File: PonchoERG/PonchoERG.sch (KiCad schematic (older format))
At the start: 1 part, among them J4 CONN_02X04

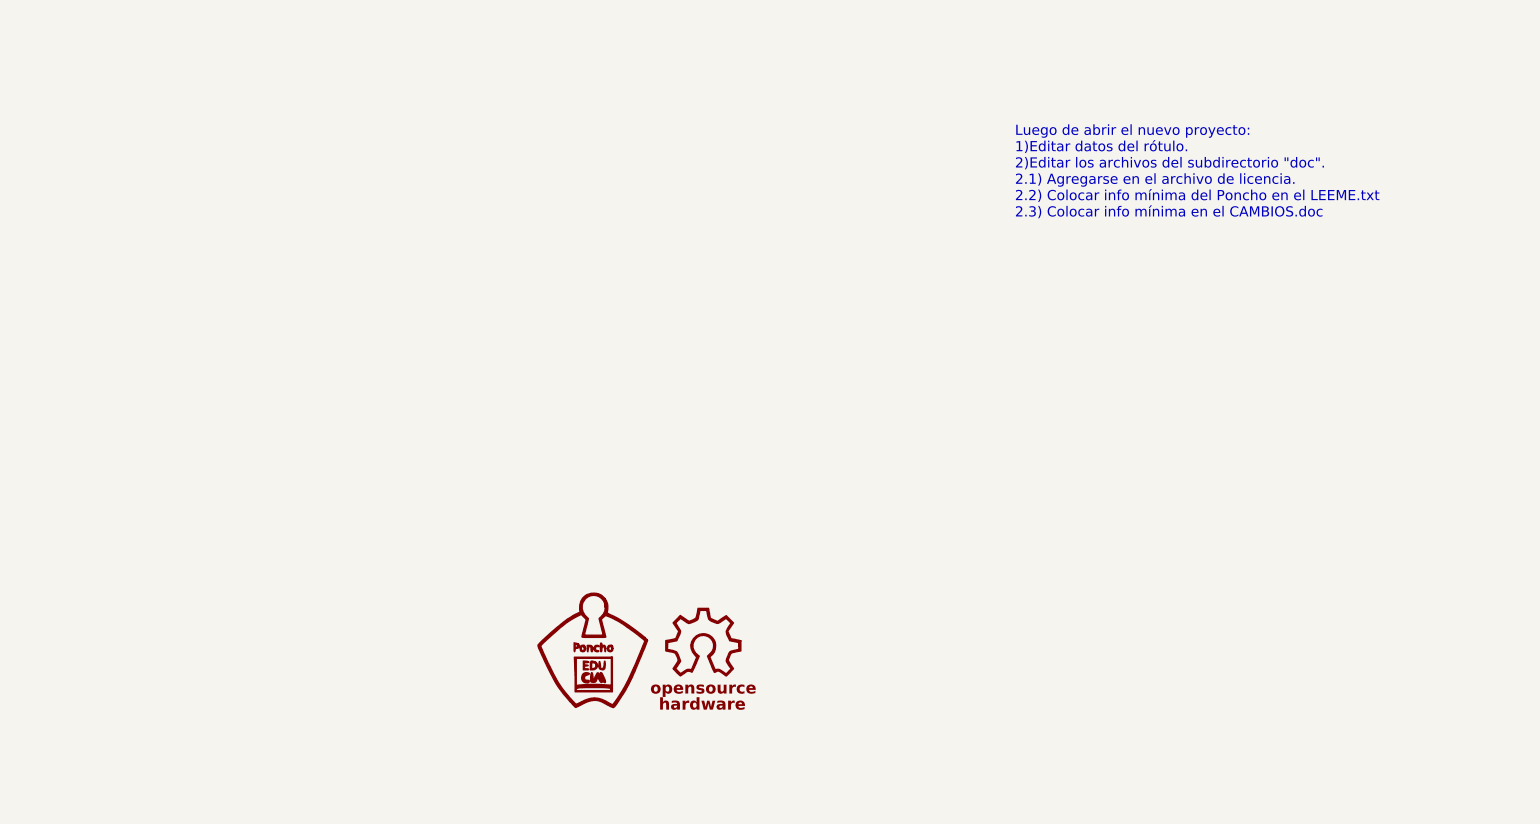
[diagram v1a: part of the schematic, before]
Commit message: Reubicación de ADS y componentes pasivos asociados. Sujeto a revisión.
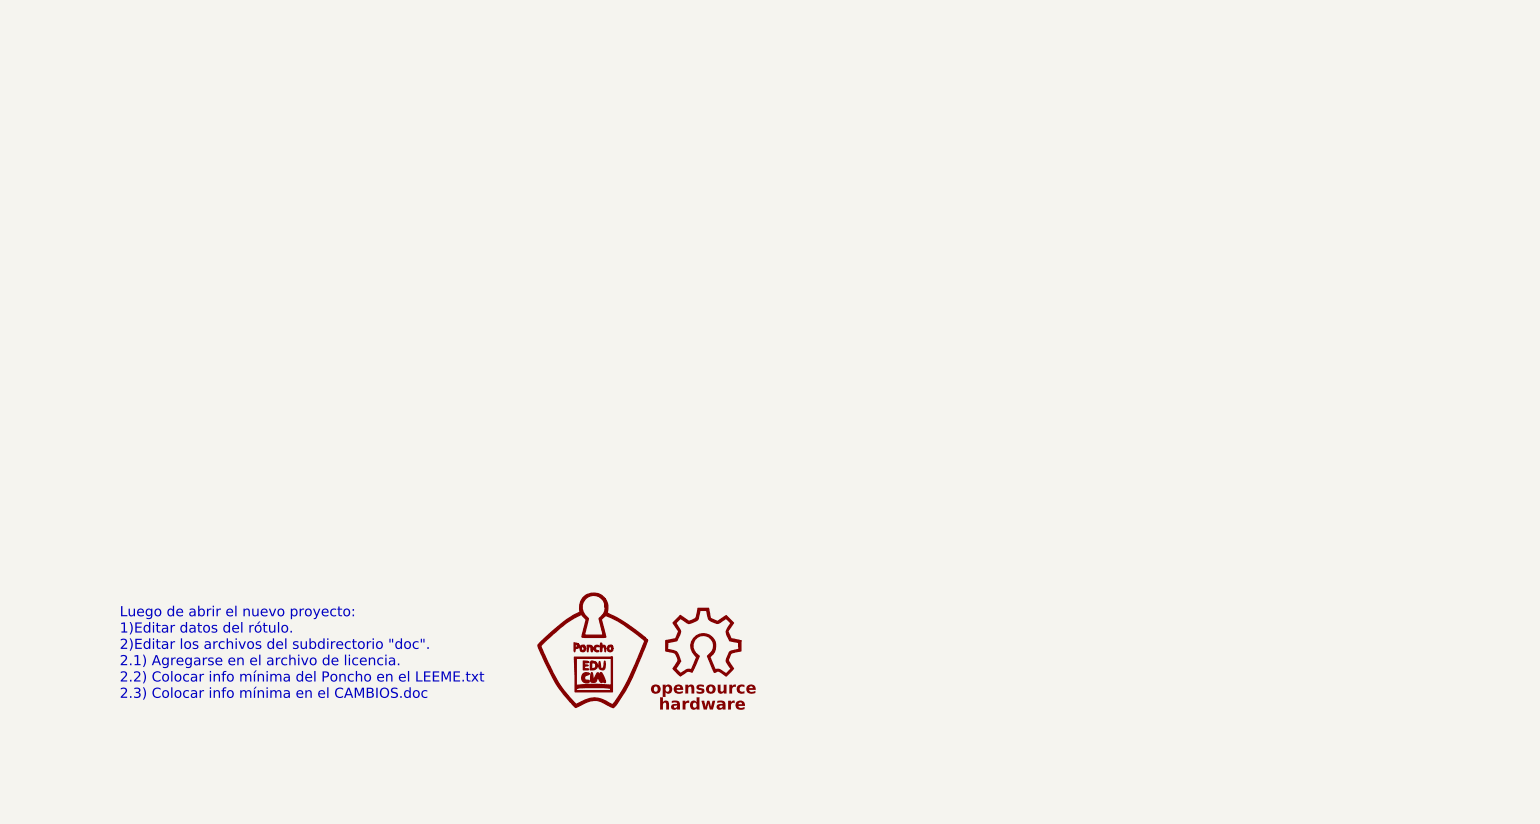
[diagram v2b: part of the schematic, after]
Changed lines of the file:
@@
 LIBS:ADuM2401
 LIBS:ADuM6401
-LIBS:CKCL44X7R1H
-LIBS:GNDD
 LIBS:NetTie
 LIBS:PonchoERG
 LIBS:PonchoERG-cache
-LIBS:Power
-LIBS:VCC
+LIBS:net-tie
+LIBS:TPD2E001
 EELAYER 25 0
 EELAYER END
@@
 	1    0    0    -1
 $EndComp
-Text Notes 12650 3450 0    60   ~ 0
+Text Notes 7350 6300 0    60   ~ 0
 Luego de abrir el nuevo proyecto:\n1)Editar datos del rótulo.\n2)Editar los archivos del subdirectorio "doc".\n2.1) Agregarse en el archivo de licencia.\n2.2) Colocar info mínima del Poncho en el LEEME.txt\n2.3) Colocar info mínima en el CAMBIOS.doc
 $Sheet
@@
 NoConn ~ 5300 6750
 Wire Wire Line
-	2900 2250 4600 2250
-Wire Wire Line
-	4600 2250 4600 4400
-Wire Wire Line
-	4600 4400 2900 4400
-Wire Wire Line
 	2900 2350 4700 2350
 Wire Wire Line
@@
 Wire Wire Line
 	5650 7550 2900 7550
+Wire Wire Line
+	2900 2250 4600 2250
+Wire Wire Line
+	4600 2250 4600 4400
+Wire Wire Line
+	4600 4400 2900 4400
 $EndSCHEMATC

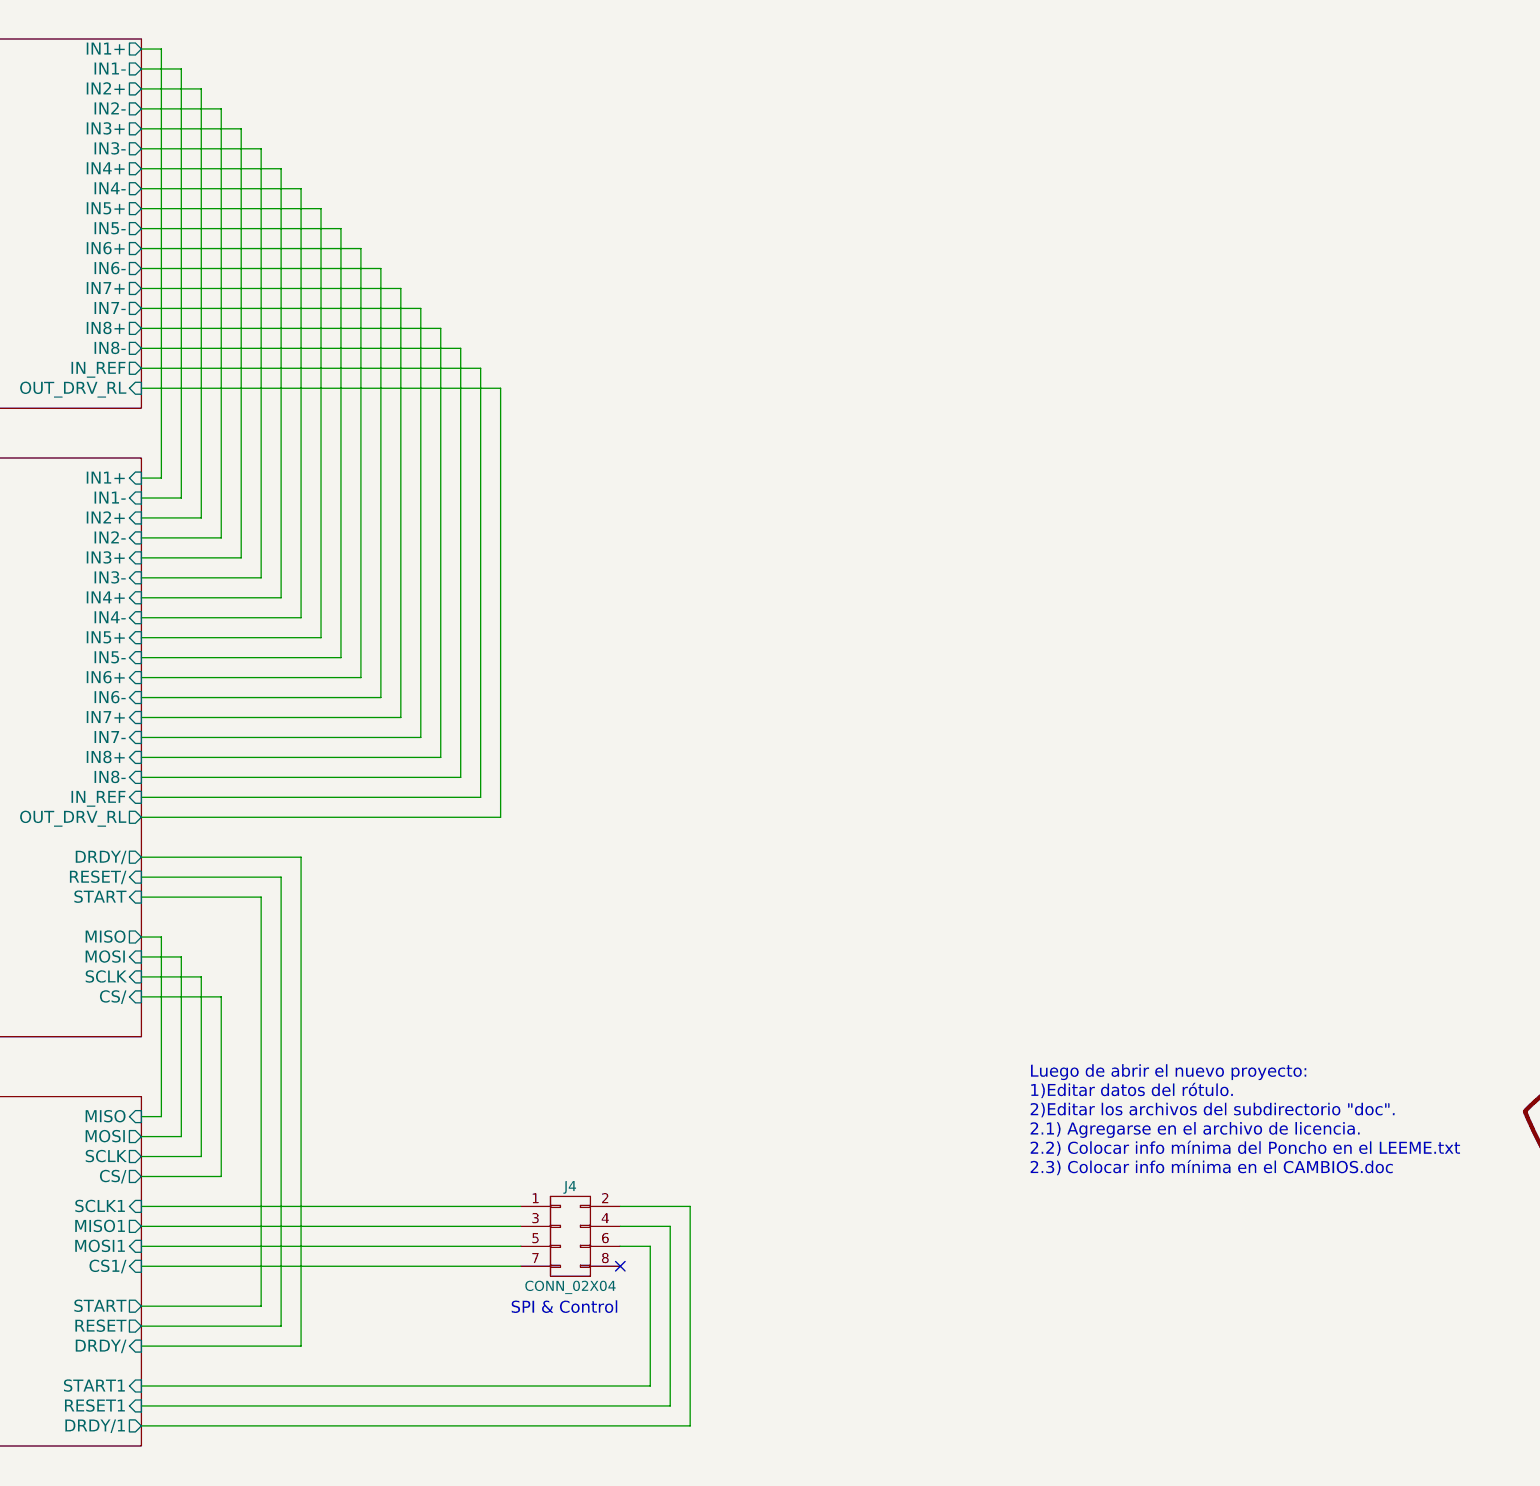
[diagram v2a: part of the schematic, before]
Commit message: Última actualización del proyecto. Creación de librería única "PonchoERG.lib" con todos los componentes. Se agregó el conector estilo CIAA para conectar SPI y alimentaciones. Se agregó carpeta con archivos para creación de lista de materiales "PonchoERG.xml" provisoria. Se modificaron todos los pines de alimentación que estaban como etiquetas con los correspondientes. Quedaría solucionar los problemas del ERC respecto a los errores de pines con el famoso PWR_FLAG.
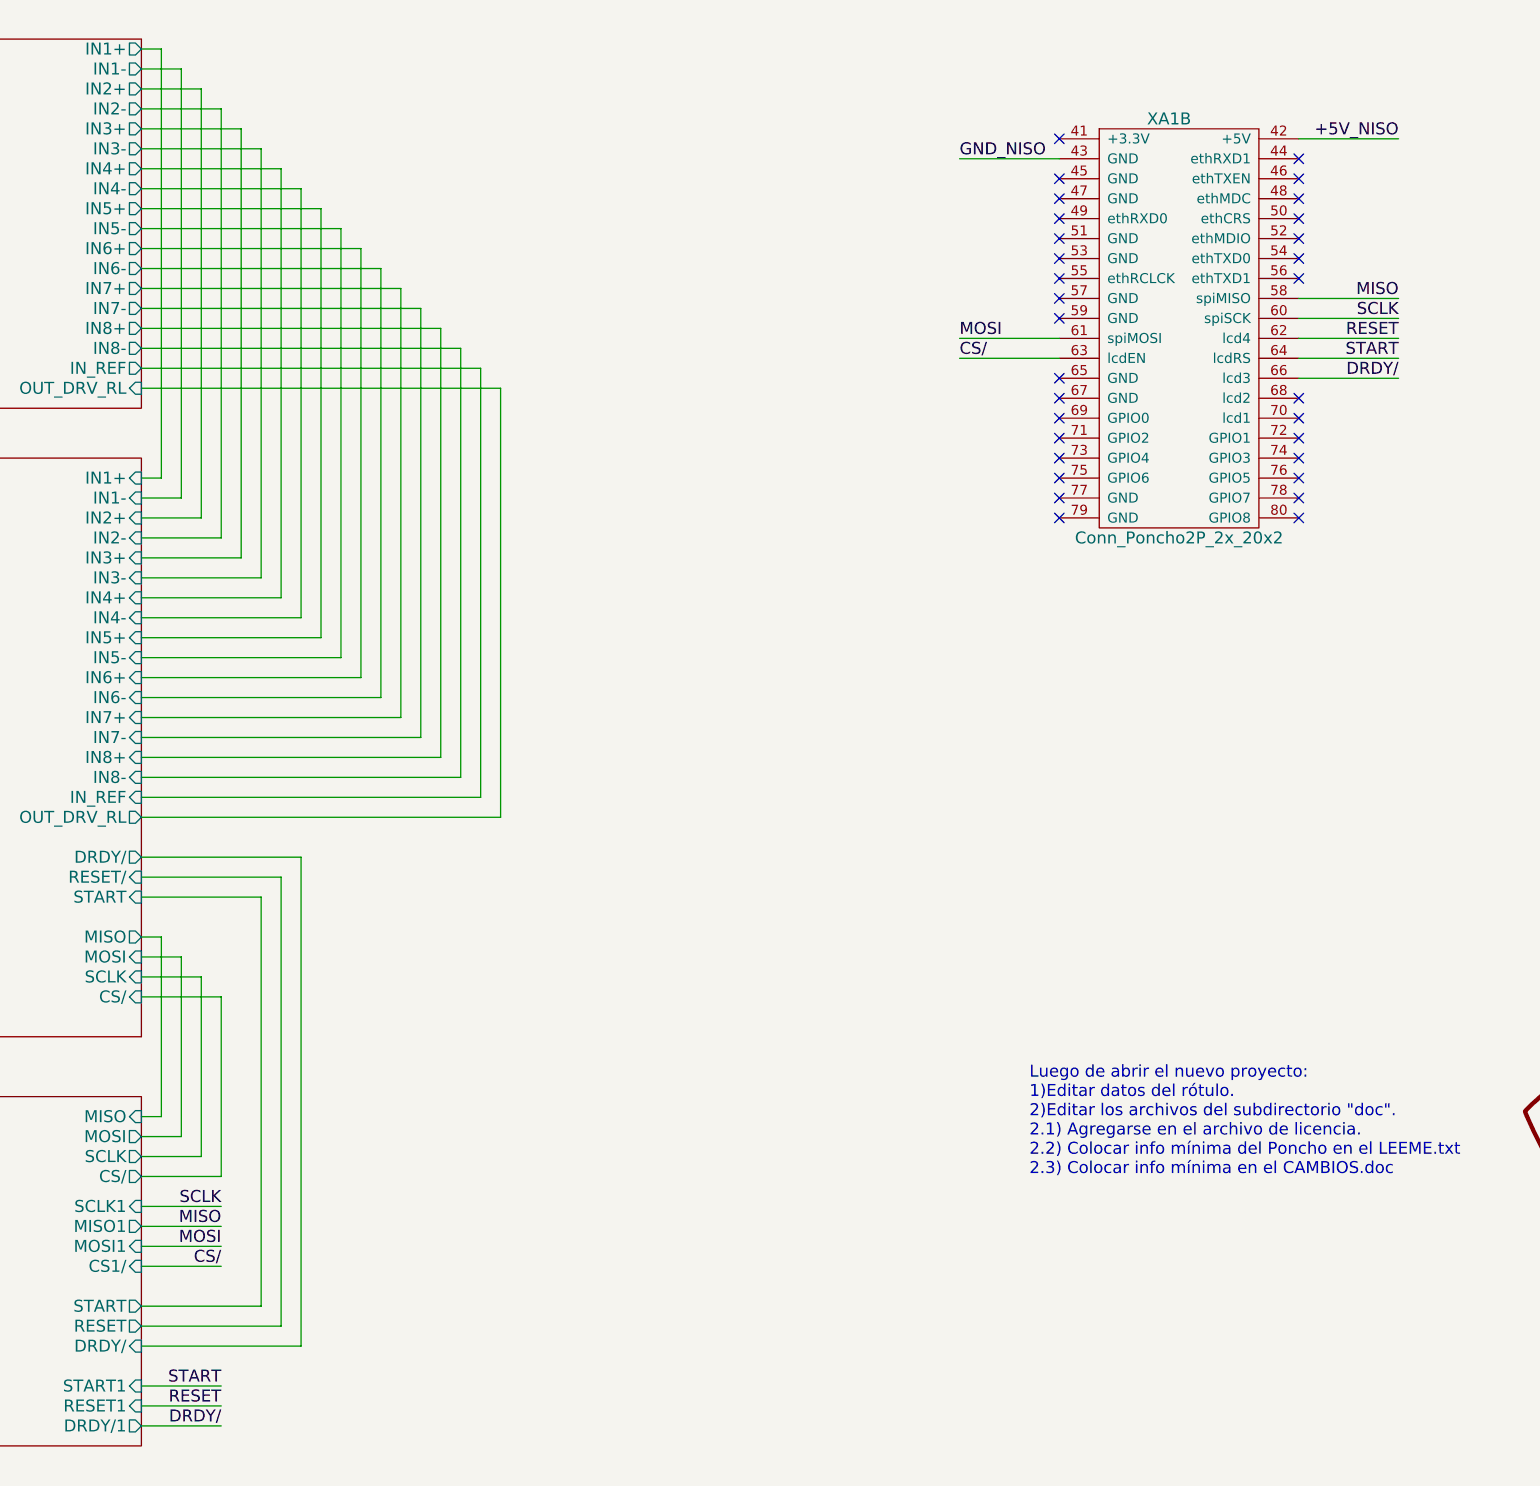
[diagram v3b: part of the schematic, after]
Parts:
- removed J4: CONN_02X04, Pin_Headers:Pin_Header_Straight_2x04, symbol CONN_02X04
- added XA1: Conn_Poncho2P_2x_20x2, symbol Conn_Poncho2P_2x_20x2
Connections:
- new net +5V_NISO: XA1.42 (+5V)
- new net CS/: XA1.63 (lcdEN)
- new net DRDY/: XA1.66 (lcd3)
- new net GND_NISO: XA1.43 (GND)
- new net MISO: XA1.58 (spiMISO)
- new net MOSI: XA1.61 (spiMOSI)
- new net RESET: XA1.62 (lcd4)
- new net SCLK: XA1.60 (spiSCK)
- new net START: XA1.64 (lcdRS)
- no-connect marks 1 -> 31
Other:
- note removed: "SPI & Control"
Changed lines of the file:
@@
 EESchema Schematic File Version 2
 LIBS:PonchoERG-rescue
-LIBS:74xgxx
-LIBS:74xx
-LIBS:ac-dc
-LIBS:actel
-LIBS:adc-dac
-LIBS:Altera
-LIBS:analog_devices
-LIBS:analog_switches
-LIBS:atmel
-LIBS:audio
-LIBS:brooktre
-LIBS:cmos_ieee
-LIBS:cmos4000
-LIBS:conn
-LIBS:contrib
-LIBS:cypress
-LIBS:dc-dc
-LIBS:device
-LIBS:digital-audio
-LIBS:diode
-LIBS:display
-LIBS:dsp
-LIBS:elec-unifil
-LIBS:ESD_Protection
-LIBS:ftdi
-LIBS:gennum
-LIBS:graphic
-LIBS:hc11
-LIBS:intel
-LIBS:interface
-LIBS:ir
-LIBS:Lattice
-LIBS:linear
-LIBS:logo
-LIBS:maxim
-LIBS:memory
-LIBS:microchip
-LIBS:microchip_dspic33dsc
-LIBS:microchip_pic10mcu
-LIBS:microchip_pic12mcu
-LIBS:microchip_pic16mcu
-LIBS:microchip_pic18mcu
-LIBS:microchip_pic32mcu
-LIBS:microcontrollers
-LIBS:motor_drivers
-LIBS:motorola
-LIBS:msp430
-LIBS:nordicsemi
-LIBS:nxp_armmcu
-LIBS:onsemi
-LIBS:opto
-LIBS:Oscillators
-LIBS:philips
+LIBS:Misc_Poncho_Grande
+LIBS:Poncho_Esqueleto
+LIBS:PonchoERG
 LIBS:power
-LIBS:Power_Management
-LIBS:powerint
-LIBS:pspice
-LIBS:references
-LIBS:regul
-LIBS:relays
-LIBS:rfcom
-LIBS:sensors
-LIBS:silabs
-LIBS:siliconi
-LIBS:stm8
-LIBS:stm32
-LIBS:supertex
-LIBS:switches
-LIBS:texas
-LIBS:transf
-LIBS:transistors
-LIBS:ttl_ieee
-LIBS:valves
-LIBS:video
-LIBS:Xicor
-LIBS:xilinx
-LIBS:Zilog
-LIBS:ADS1299
-LIBS:ADuM2401
-LIBS:ADuM6401
-LIBS:NetTie
-LIBS:PonchoERG
 LIBS:PonchoERG-cache
-LIBS:net-tie
-LIBS:TPD2E001
 EELAYER 25 0
 EELAYER END
@@
 Wire Wire Line
 	3700 7150 2900 7150
+Wire Wire Line
+	2900 2350 4700 2350
+Wire Wire Line
+	4700 2350 4700 4500
+Wire Wire Line
+	4700 4500 2900 4500
+Wire Wire Line
+	2900 2250 4600 2250
+Wire Wire Line
+	4600 2250 4600 4400
+Wire Wire Line
+	4600 4400 2900 4400
 $Comp
-L CONN_02X04 J4
-U 1 1 57C36F2F
-P 5050 6600
-F 0 "J4" H 5050 6850 50  0000 C CNN
-F 1 "CONN_02X04" H 5050 6350 50  0000 C CNN
-F 2 "Pin_Headers:Pin_Header_Straight_2x04" H 5050 5400 50  0001 C CNN
-F 3 "" H 5050 5400 50  0000 C CNN
-	1    5050 6600
+L Conn_Poncho2P_2x_20x2 XA1
+U 2 1 57CB029C
+P 7750 1400
+F 0 "XA1" H 8050 1800 60  0000 C CNN
+F 1 "Conn_Poncho2P_2x_20x2" H 8100 -300 60  0000 C CNN
+F 2 "" H 7750 1400 60  0000 C CNN
+F 3 "" H 7750 1400 60  0000 C CNN
+	2    7750 1400
 	1    0    0    -1
 $EndComp
-NoConn ~ 5300 6750
-Wire Wire Line
-	2900 2350 4700 2350
-Wire Wire Line
-	4700 2350 4700 4500
-Wire Wire Line
-	4700 4500 2900 4500
-Text Notes 4750 7000 0    60   ~ 0
-SPI & Control
-Wire Wire Line
-	2900 6450 4800 6450
-Wire Wire Line
-	2900 6550 4800 6550
-Wire Wire Line
-	2900 6650 4800 6650
-Wire Wire Line
-	2900 6750 4800 6750
-Wire Wire Line
-	5300 6650 5450 6650
-Wire Wire Line
-	5450 6650 5450 7350
-Wire Wire Line
-	5450 7350 2900 7350
-Wire Wire Line
-	2900 7450 5550 7450
-Wire Wire Line
-	5550 7450 5550 6550
-Wire Wire Line
-	5550 6550 5300 6550
-Wire Wire Line
-	5300 6450 5650 6450
-Wire Wire Line
-	5650 6450 5650 7550
-Wire Wire Line
-	5650 7550 2900 7550
-Wire Wire Line
-	2900 2250 4600 2250
-Wire Wire Line
-	4600 2250 4600 4400
-Wire Wire Line
-	4600 4400 2900 4400
+Wire Wire Line
+	8700 1100 9200 1100
+Wire Wire Line
+	7500 1200 7000 1200
+Text Label 9200 1100 2    60   ~ 0
++5V_NISO
+Text Label 7000 1200 0    60   ~ 0
+GND_NISO
+Wire Wire Line
+	8700 1900 9200 1900
+Wire Wire Line
+	8700 2000 9200 2000
+Wire Wire Line
+	7500 2100 7000 2100
+Wire Wire Line
+	8700 2100 9200 2100
+Wire Wire Line
+	7500 2200 7000 2200
+Wire Wire Line
+	8700 2200 9200 2200
+Wire Wire Line
+	8700 2300 9200 2300
+Text Label 9200 1900 2    60   ~ 0
+MISO
+Text Label 9200 2000 2    60   ~ 0
+SCLK
+Text Label 9200 2100 2    60   ~ 0
+RESET
+Text Label 9200 2200 2    60   ~ 0
+START
+Text Label 7000 2200 0    60   ~ 0
+CS/
+Text Label 7000 2100 0    60   ~ 0
+MOSI
+Text Label 9200 2300 2    60   ~ 0
+DRDY/
+Wire Wire Line
+	2900 6450 3300 6450
+Wire Wire Line
+	2900 6550 3300 6550
+Wire Wire Line
+	2900 6650 3300 6650
+Wire Wire Line
+	2900 6750 3300 6750
+Wire Wire Line
+	2900 7350 3300 7350
+Wire Wire Line
+	2900 7450 3300 7450
+Wire Wire Line
+	2900 7550 3300 7550
+Text Label 3300 6450 2    60   ~ 0
+SCLK
+Text Label 3300 6550 2    60   ~ 0
+MISO
+Text Label 3300 6650 2    60   ~ 0
+MOSI
+Text Label 3300 6750 2    60   ~ 0
+CS/
+Text Label 3300 7350 2    60   ~ 0
+START
+Text Label 3300 7450 2    60   ~ 0
+RESET
+Text Label 3300 7550 2    60   ~ 0
+DRDY/
+NoConn ~ 7500 1100
+NoConn ~ 7500 1300
+NoConn ~ 7500 1400
+NoConn ~ 7500 1500
+NoConn ~ 7500 1600
+NoConn ~ 7500 1700
+NoConn ~ 7500 1800
+NoConn ~ 7500 1900
+NoConn ~ 7500 2000
+NoConn ~ 7500 2300
+NoConn ~ 7500 2400
+NoConn ~ 7500 2500
+NoConn ~ 7500 2600
+NoConn ~ 7500 2700
+NoConn ~ 7500 2800
+NoConn ~ 7500 2900
+NoConn ~ 7500 3000
+NoConn ~ 8700 3000
+NoConn ~ 8700 2900
+NoConn ~ 8700 2800
+NoConn ~ 8700 2700
+NoConn ~ 8700 2600
+NoConn ~ 8700 2500
+NoConn ~ 8700 2400
+NoConn ~ 8700 1800
+NoConn ~ 8700 1700
+NoConn ~ 8700 1600
+NoConn ~ 8700 1500
+NoConn ~ 8700 1400
+NoConn ~ 8700 1300
+NoConn ~ 8700 1200
 $EndSCHEMATC
